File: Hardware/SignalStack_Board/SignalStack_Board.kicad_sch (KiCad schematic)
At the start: 70 parts, among them Q1 SI4156DY, Q2 SI4156DY, Q3 SI4156DY, Q4 SI4156DY, Q5 SI4156DY, Q6 SI4156DY, Q7 SI4156DY, Q8 SI4156DY, Q9 Q_PMOS_DGS, SW1 SW_Push, SW2 SW_Push, U1 OKI, U10 74LVC2G04, U2 Raspberry_Pi, U4 TSR_1-2450, U5 IRS2005S, U6 IRS2005S, U7 74LVC2G04, U8 IRS2005S, U9 IRS2005S

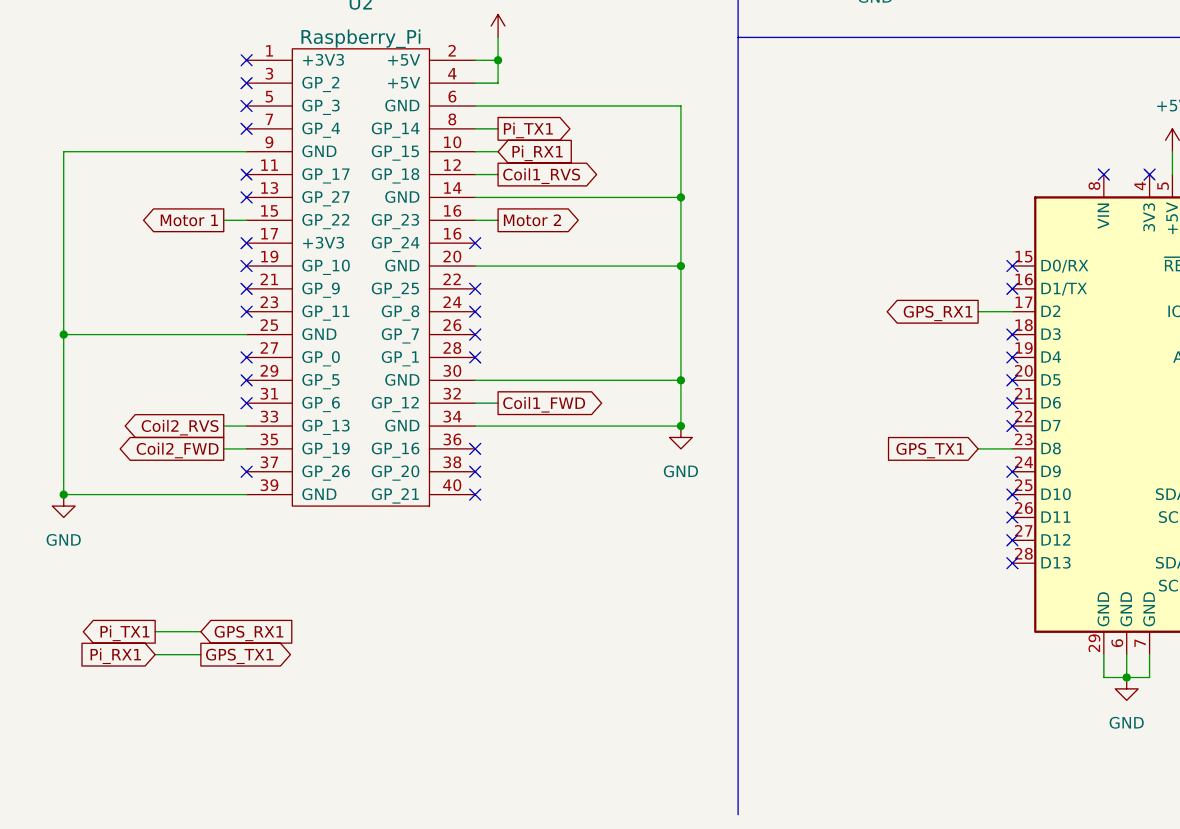
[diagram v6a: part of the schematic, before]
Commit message: Added 2nd serial line
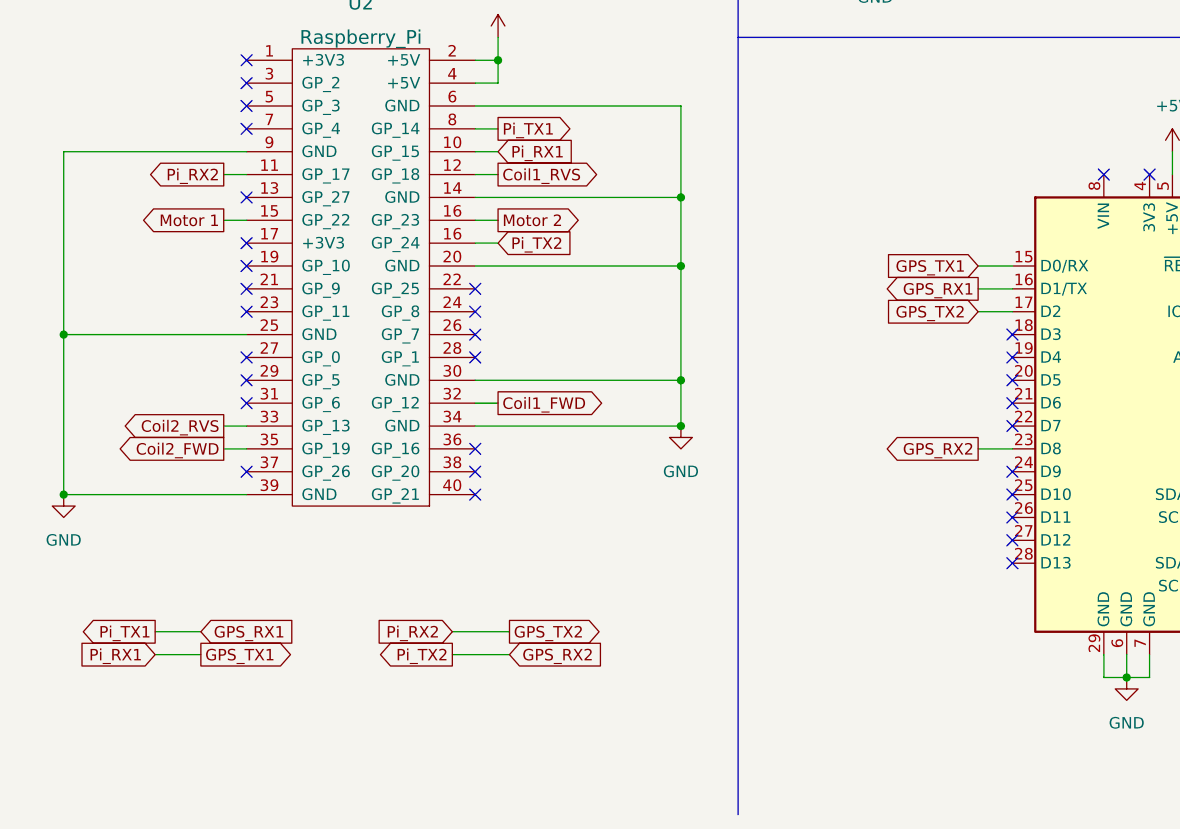
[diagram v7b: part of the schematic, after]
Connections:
- net GPS_RX1: now also A1.16 (D1/TX); no longer A1.17 (D2)
- net GPS_TX1: now also A1.15 (D0/RX); no longer A1.23 (D8)
- net GPS_TX2: now reaches U2.11 (GP_17)
- net GPS_TX2: now also A1.17 (D2)
- new net GPS_RX2: A1.23 (D8), U2.16 (GP_24)
- no-connect marks 46 -> 42
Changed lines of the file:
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@@
   (no_connect (at 36.83 129.54))
   (no_connect (at 121.92 160.02))
-  (no_connect (at 121.92 137.16))
   (no_connect (at 62.23 142.24))
   (no_connect (at 36.83 114.3))
-  (no_connect (at 121.92 139.7))
   (no_connect (at 62.23 139.7))
   (no_connect (at 36.83 152.4))
@@
   (no_connect (at 121.92 154.94))
   (no_connect (at 121.92 162.56))
-  (no_connect (at 62.23 134.62))
   (no_connect (at 147.32 165.1))
   (no_connect (at 147.32 160.02))
@@
   (no_connect (at 36.83 160.02))
   (no_connect (at 137.16 127))
-  (no_connect (at 36.83 127))
   (no_connect (at 36.83 121.92))
   (no_connect (at 147.32 157.48))
@@
     (stroke (width 0) (type default) (color 0 0 0 0))
   )
+  (wire (pts (xy 34.29 127) (xy 36.83 127))
+    (stroke (width 0) (type default) (color 0 0 0 0))
+  )
   (wire (pts (xy 116.84 48.26) (xy 133.985 48.26))
     (stroke (width 0) (type default) (color 0 0 0 0))
   )
+  (wire (pts (xy 59.69 180.34) (xy 66.04 180.34))
+    (stroke (width 0) (type default) (color 0 0 0 0))
+  )
   (polyline (pts (xy 177.8 111.76) (xy 177.8 166.37))
     (stroke (width 0) (type default) (color 0 0 0 0))
@@
     (stroke (width 0) (type default) (color 0 0 0 0))
   )
+  (wire (pts (xy 118.11 137.16) (xy 121.92 137.16))
+    (stroke (width 0) (type default) (color 0 0 0 0))
+  )
+  (wire (pts (xy 106.68 36.83) (xy 109.22 36.83))
+    (stroke (width 0) (type default) (color 0 0 0 0))
+  )
+  (wire (pts (xy 62.23 132.08) (xy 64.77 132.08))
+    (stroke (width 0) (type default) (color 0 0 0 0))
+  )
+  (wire (pts (xy 62.23 137.16) (xy 85.09 137.16))
+    (stroke (width 0) (type default) (color 0 0 0 0))
+  )
+  (wire (pts (xy 54.61 22.86) (xy 54.61 25.4))
+    (stroke (width 0) (type default) (color 0 0 0 0))
+  )
+  (wire (pts (xy 224.79 146.05) (xy 224.79 143.51))
+    (stroke (width 0) (type default) (color 0 0 0 0))
+  )
+  (wire (pts (xy 59.69 177.8) (xy 66.04 177.8))
+    (stroke (width 0) (type default) (color 0 0 0 0))
+  )
+  (wire (pts (xy 82.55 63.5) (xy 85.09 63.5))
+    (stroke (width 0) (type default) (color 0 0 0 0))
+  )
+  (polyline (pts (xy 11.43 77.47) (xy 91.44 77.47))
+    (stroke (width 0) (type default) (color 0 0 0 0))
+  )
+  (wire (pts (xy 235.585 26.67) (xy 235.585 20.32))
+    (stroke (width 0) (type default) (color 0 0 0 0))
+  )
+  (wire (pts (xy 104.775 78.74) (xy 106.68 78.74))
+    (stroke (width 0) (type default) (color 0 0 0 0))
+  )
   (wire (pts (xy 118.11 157.48) (xy 121.92 157.48))
     (stroke (width 0) (type default) (color 0 0 0 0))
   )
-  (wire (pts (xy 106.68 36.83) (xy 109.22 36.83))
-    (stroke (width 0) (type default) (color 0 0 0 0))
-  )
-  (wire (pts (xy 62.23 132.08) (xy 64.77 132.08))
-    (stroke (width 0) (type default) (color 0 0 0 0))
-  )
-  (wire (pts (xy 62.23 137.16) (xy 85.09 137.16))
-    (stroke (width 0) (type default) (color 0 0 0 0))
-  )
-  (wire (pts (xy 54.61 22.86) (xy 54.61 25.4))
-    (stroke (width 0) (type default) (color 0 0 0 0))
-  )
-  (wire (pts (xy 224.79 146.05) (xy 224.79 143.51))
-    (stroke (width 0) (type default) (color 0 0 0 0))
-  )
-  (wire (pts (xy 82.55 63.5) (xy 85.09 63.5))
-    (stroke (width 0) (type default) (color 0 0 0 0))
-  )
-  (polyline (pts (xy 11.43 77.47) (xy 91.44 77.47))
-    (stroke (width 0) (type default) (color 0 0 0 0))
-  )
-  (wire (pts (xy 235.585 26.67) (xy 235.585 20.32))
-    (stroke (width 0) (type default) (color 0 0 0 0))
-  )
-  (wire (pts (xy 104.775 78.74) (xy 106.68 78.74))
-    (stroke (width 0) (type default) (color 0 0 0 0))
-  )
   (wire (pts (xy 64.77 116.84) (xy 62.23 116.84))
     (stroke (width 0) (type default) (color 0 0 0 0))
@@
     (stroke (width 0) (type default) (color 0 0 0 0))
   )
+  (wire (pts (xy 62.23 134.62) (xy 64.77 134.62))
+    (stroke (width 0) (type default) (color 0 0 0 0))
+  )
   (wire (pts (xy 245.745 48.26) (xy 245.745 49.53))
     (stroke (width 0) (type default) (color 0 0 0 0))
@@
     (stroke (width 0) (type default) (color 0 0 0 0))
   )
+  (wire (pts (xy 118.11 142.24) (xy 121.92 142.24))
+    (stroke (width 0) (type default) (color 0 0 0 0))
+  )
   (wire (pts (xy 154.305 39.37) (xy 154.305 35.56))
     (stroke (width 0) (type default) (color 0 0 0 0))
@@
     (stroke (width 0) (type default) (color 0 0 0 0))
   )
-  (wire (pts (xy 118.11 142.24) (xy 121.92 142.24))
+  (wire (pts (xy 118.11 139.7) (xy 121.92 139.7))
     (stroke (width 0) (type default) (color 0 0 0 0))
   )
@@
     )
   )
+  (global_label "Pi_RX2" (shape input) (at 59.69 177.8 180) (fields_autoplaced)
+    (effects (font (size 1.27 1.27)) (justify right))
+    (property "Intersheet References" "${INTERSHEET_REFS}" (id 0) (at 50.7455 177.7206 0)
+      (effects (font (size 1.27 1.27)) (justify right) hide)
+    )
+  )
+  (global_label "Pi_TX2" (shape output) (at 59.69 180.34 180) (fields_autoplaced)
+    (effects (font (size 1.27 1.27)) (justify right))
+    (property "Intersheet References" "${INTERSHEET_REFS}" (id 0) (at 51.0479 180.2606 0)
+      (effects (font (size 1.27 1.27)) (justify right) hide)
+    )
+  )
   (global_label "Coil2_FWD" (shape output) (at 34.29 157.48 180) (fields_autoplaced)
     (effects (font (size 1.27 1.27)) (justify right))
@@
     )
   )
-  (global_label "GPS_TX1" (shape input) (at 118.11 157.48 180) (fields_autoplaced)
-    (effects (font (size 1.27 1.27)) (justify right))
-    (property "Intersheet References" "${INTERSHEET_REFS}" (id 0) (at 107.5931 157.4006 0)
+  (global_label "GPS_TX1" (shape input) (at 118.11 137.16 180) (fields_autoplaced)
+    (effects (font (size 1.27 1.27)) (justify right))
+    (property "Intersheet References" "${INTERSHEET_REFS}" (id 0) (at 107.5931 137.0806 0)
       (effects (font (size 1.27 1.27)) (justify right) hide)
     )
@@
     )
   )
+  (global_label "Pi_TX2" (shape input) (at 64.77 134.62 0) (fields_autoplaced)
+    (effects (font (size 1.27 1.27)) (justify left))
+    (property "Intersheet References" "${INTERSHEET_REFS}" (id 0) (at 73.4121 134.5406 0)
+      (effects (font (size 1.27 1.27)) (justify left) hide)
+    )
+  )
+  (global_label "GPS_RX2" (shape input) (at 66.04 180.34 0) (fields_autoplaced)
+    (effects (font (size 1.27 1.27)) (justify left))
+    (property "Intersheet References" "${INTERSHEET_REFS}" (id 0) (at 76.8593 180.2606 0)
+      (effects (font (size 1.27 1.27)) (justify left) hide)
+    )
+  )
   (global_label "Pi_TX1" (shape output) (at 64.77 121.92 0) (fields_autoplaced)
     (effects (font (size 1.27 1.27)) (justify left))
@@
     )
   )
+  (global_label "GPS_RX2" (shape output) (at 118.11 157.48 180) (fields_autoplaced)
+    (effects (font (size 1.27 1.27)) (justify right))
+    (property "Intersheet References" "${INTERSHEET_REFS}" (id 0) (at 107.2907 157.4006 0)
+      (effects (font (size 1.27 1.27)) (justify right) hide)
+    )
+  )
   (global_label "Motor 2" (shape input) (at 201.93 128.27 0) (fields_autoplaced)
     (effects (font (size 1.27 1.27)) (justify left))
@@
     )
   )
+  (global_label "Pi_RX2" (shape output) (at 34.29 127 180) (fields_autoplaced)
+    (effects (font (size 1.27 1.27)) (justify right))
+    (property "Intersheet References" "${INTERSHEET_REFS}" (id 0) (at 25.3455 126.9206 0)
+      (effects (font (size 1.27 1.27)) (justify right) hide)
+    )
+  )
   (global_label "Coil2_RVS" (shape input) (at 273.05 78.74 0) (fields_autoplaced)
     (effects (font (size 1.27 1.27)) (justify left))
@@
     )
   )
+  (global_label "GPS_TX2" (shape output) (at 66.04 177.8 0) (fields_autoplaced)
+    (effects (font (size 1.27 1.27)) (justify left))
+    (property "Intersheet References" "${INTERSHEET_REFS}" (id 0) (at 76.5569 177.7206 0)
+      (effects (font (size 1.27 1.27)) (justify left) hide)
+    )
+  )
   (global_label "Motor 1" (shape output) (at 34.29 132.08 180) (fields_autoplaced)
     (effects (font (size 1.27 1.27)) (justify right))
@@
     )
   )
-  (global_label "GPS_RX1" (shape output) (at 118.11 142.24 180) (fields_autoplaced)
-    (effects (font (size 1.27 1.27)) (justify right))
-    (property "Intersheet References" "${INTERSHEET_REFS}" (id 0) (at 107.2907 142.3194 0)
-      (effects (font (size 1.27 1.27)) (justify right) hide)
-    )
+  (global_label "GPS_TX2" (shape input) (at 118.11 142.24 180) (fields_autoplaced)
+    (effects (font (size 1.27 1.27)) (justify right))
+    (property "Intersheet References" "${INTERSHEET_REFS}" (id 0) (at 107.5931 142.1606 0)
+      (effects (font (size 1.27 1.27)) (justify right) hide)
+    )
+  )
+  (global_label "GPS_RX1" (shape output) (at 118.11 139.7 180) (fields_autoplaced)
+    (effects (font (size 1.27 1.27)) (justify right))
+    (property "Intersheet References" "${INTERSHEET_REFS}" (id 0) (at 107.2907 139.7794 0)
+      (effects (font (size 1.27 1.27)) (justify right) hide)
+    )
